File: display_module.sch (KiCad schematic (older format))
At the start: 110 parts, among them J3 F52R-1A7H1-11020, J4 46756-1001, Q3 BSS138APW, Q4 BSS138APW, Q5 BSS138APW, Q6 BSS138APW, U7 LT9611UXC, U8 NTS0102GT, Y1 ABM8G-24.000MHZ-18-D2Y-T

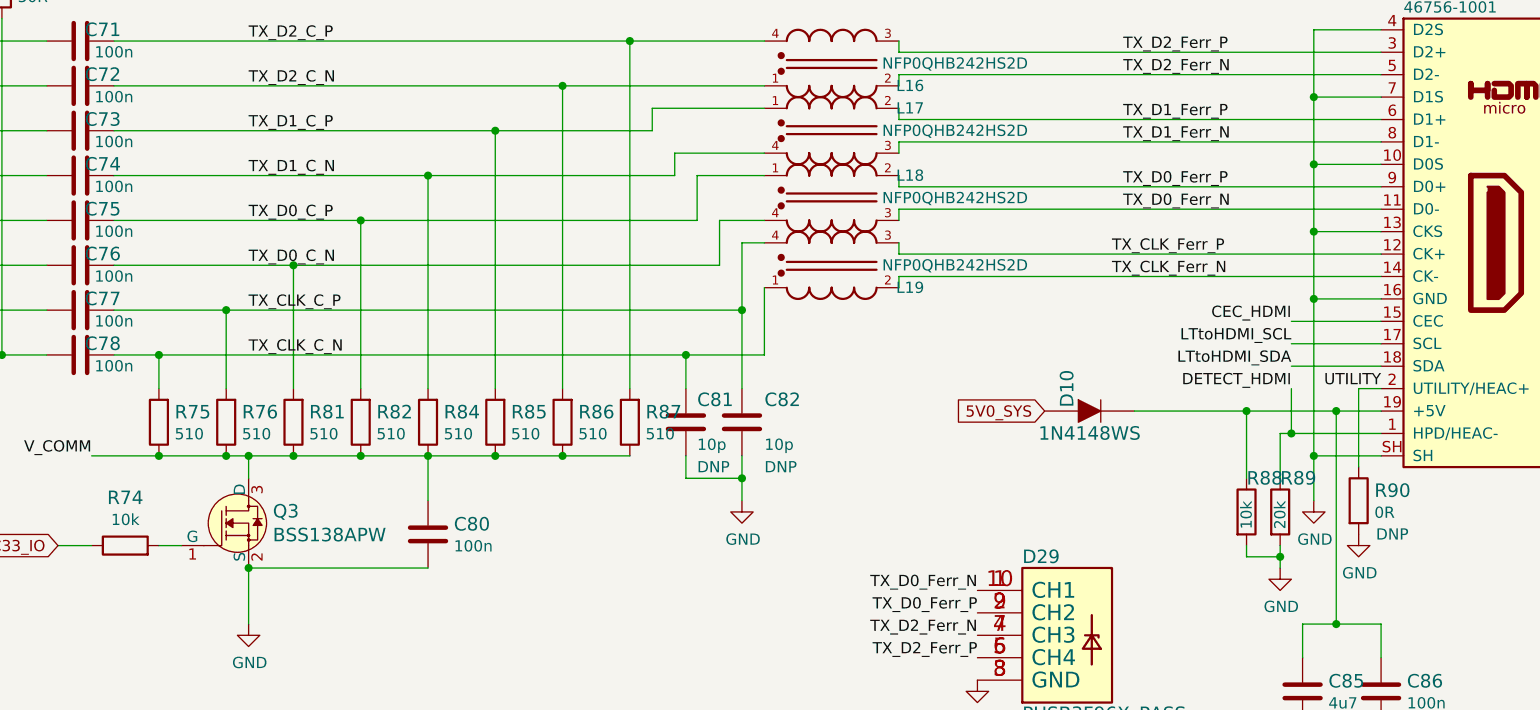
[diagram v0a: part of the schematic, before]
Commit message: Adjusted HDMI-side layout around Lontium chip
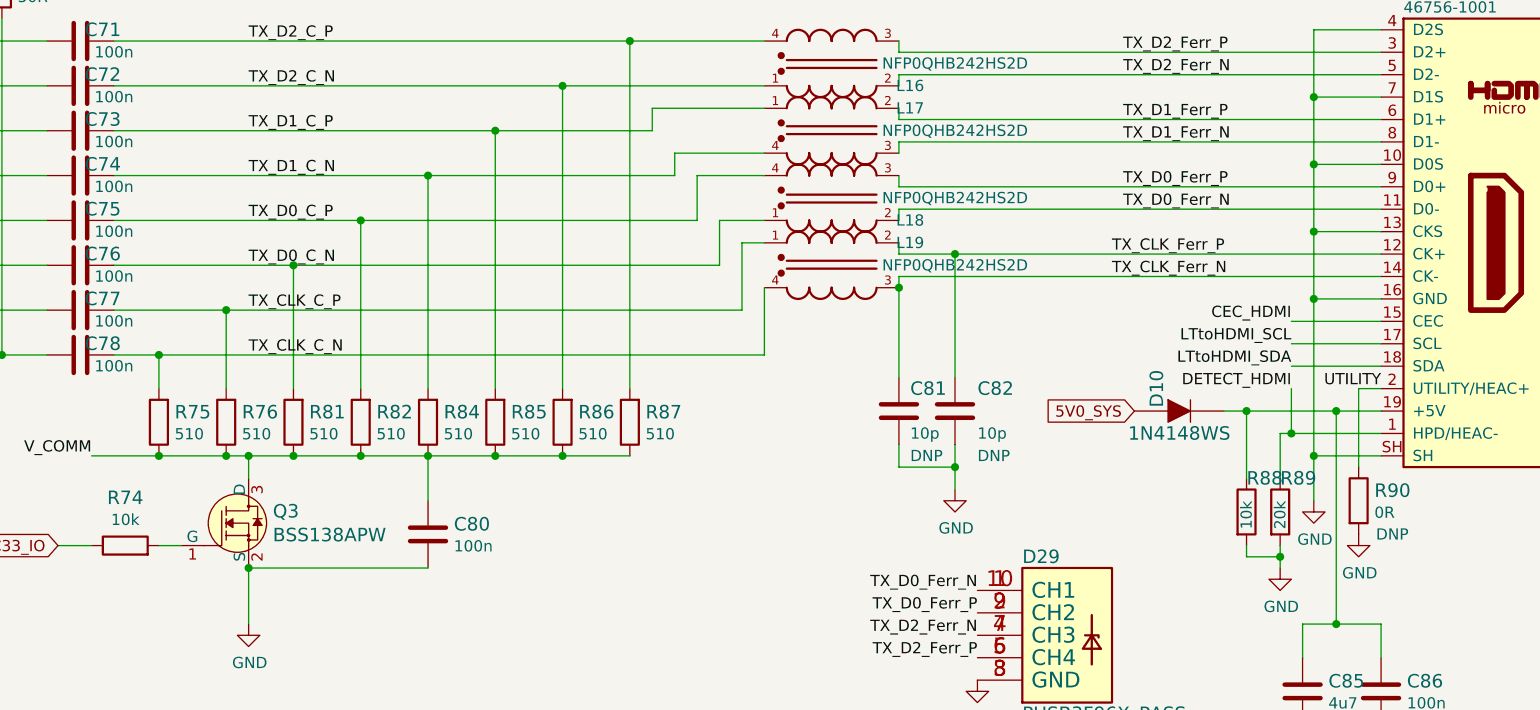
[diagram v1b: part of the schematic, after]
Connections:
- net TX_CLK_C_N: now also L19.4; no longer C81.1, L19.1
- net TX_CLK_C_P: now also L19.1; no longer C82.1, L19.4
- net TX_CLK_Ferr_N: now also C81.1, L19.3; no longer L19.2
- net TX_CLK_Ferr_P: now also C82.1, L19.2; no longer L19.3
- net TX_D0_C_N: now also L18.1; no longer L18.4
- net TX_D0_C_P: now also L18.4; no longer L18.1
- net TX_D0_Ferr_N: now also L18.2; no longer L18.3
- net TX_D0_Ferr_P: now also L18.3; no longer L18.2
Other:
- moved on the sheet: C81, C82, D10
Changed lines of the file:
@@
 F 5 "MURATA" H 12700 2126 50  0001 C CNN "Manufacturer"
 	1    12700 1900
-	1    0    0    -1
+	1    0    0    1
 $EndComp
 Wire Wire Line
@@
 F 5 "MURATA" H 12700 2426 50  0001 C CNN "Manufacturer"
 	1    12700 2200
-	1    0    0    1
+	1    0    0    -1
 $EndComp
 Wire Wire Line
@@
 L sc606-baseboard:C_10p_0402 C81
 U 1 1 64B46E2F
-P 12050 2900
-F 0 "C81" H 12100 3000 60  0000 L CNN
-F 1 "C_10p_0402" H 12050 2750 60  0001 C CNN
-F 2 "sc606-baseboard-footprints:0402-cap" H 12250 3100 60  0001 L CNN
-F 3 "" H 12050 2900 50  0001 C CNN
-F 4 "MULTICOMP" H 12250 3300 60  0001 L CNN "Manufacturer"
-F 5 "MC0402N100D500CT" H 12250 3200 60  0001 L CNN "MPN"
-F 6 "10p" H 12100 2800 50  0000 L CNN "Val"
-F 7 "DNP" H 12100 2700 50  0000 L CNN "DNP"
-	1    12050 2900
-	1    0    0    -1
-$EndComp
-Wire Wire Line
-	12050 2750 12050 2600
-Wire Wire Line
-	12300 2750 12300 2400
-Connection ~ 12300 2400
+P 13000 2850
+F 0 "C81" H 13050 2950 60  0000 L CNN
+F 1 "C_10p_0402" H 13000 2700 60  0001 C CNN
+F 2 "sc606-baseboard-footprints:0402-cap" H 13200 3050 60  0001 L CNN
+F 3 "" H 13000 2850 50  0001 C CNN
+F 4 "MULTICOMP" H 13200 3250 60  0001 L CNN "Manufacturer"
+F 5 "MC0402N100D500CT" H 13200 3150 60  0001 L CNN "MPN"
+F 6 "10p" H 13050 2750 50  0000 L CNN "Val"
+F 7 "DNP" H 13050 2650 50  0000 L CNN "DNP"
+	1    13000 2850
+	1    0    0    -1
+$EndComp
+Wire Wire Line
+	13000 2700 13000 2300
+Wire Wire Line
+	13250 2700 13250 2150
 Wire Wire Line
 	10000 2400 12300 2400
-Connection ~ 12050 2600
-Wire Wire Line
-	12050 2600 12400 2600
-Wire Wire Line
-	9700 2600 12050 2600
 $Comp
 L sc606-baseboard:GND #PWR077
 U 1 1 64CA82FA
-P 12300 3250
-F 0 "#PWR077" H 12300 3000 50  0001 C CNN
-F 1 "GND" H 12305 3077 50  0000 C CNN
-F 2 "" H 12300 3250 50  0001 C CNN
-F 3 "" H 12300 3250 50  0001 C CNN
-	1    12300 3250
-	1    0    0    -1
-$EndComp
-Wire Wire Line
-	12300 3250 12300 3150
-Wire Wire Line
-	12050 3150 12300 3150
-Connection ~ 12300 3150
-Wire Wire Line
-	12300 3150 12300 3050
-Wire Wire Line
-	12050 3150 12050 3050
+P 13250 3200
+F 0 "#PWR077" H 13250 2950 50  0001 C CNN
+F 1 "GND" H 13255 3027 50  0000 C CNN
+F 2 "" H 13250 3200 50  0001 C CNN
+F 3 "" H 13250 3200 50  0001 C CNN
+	1    13250 3200
+	1    0    0    -1
+$EndComp
+Wire Wire Line
+	13250 3200 13250 3100
+Wire Wire Line
+	13000 3100 13250 3100
+Connection ~ 13250 3100
+Wire Wire Line
+	13250 3100 13250 3000
+Wire Wire Line
+	13000 3100 13000 3000
 $Comp
 L sc606-baseboard:C_10p_0402 C82
 U 1 1 64B47860
-P 12300 2900
-F 0 "C82" H 12400 3000 60  0000 L CNN
-F 1 "C_10p_0402" H 12300 2750 60  0001 C CNN
-F 2 "sc606-baseboard-footprints:0402-cap" H 12500 3100 60  0001 L CNN
-F 3 "" H 12300 2900 50  0001 C CNN
-F 4 "MULTICOMP" H 12500 3300 60  0001 L CNN "Manufacturer"
-F 5 "MC0402N100D500CT" H 12500 3200 60  0001 L CNN "MPN"
-F 6 "10p" H 12400 2800 50  0000 L CNN "Val"
-F 7 "DNP" H 12400 2700 50  0000 L CNN "DNP"
-	1    12300 2900
+P 13250 2850
+F 0 "C82" H 13350 2950 60  0000 L CNN
+F 1 "C_10p_0402" H 13250 2700 60  0001 C CNN
+F 2 "sc606-baseboard-footprints:0402-cap" H 13450 3050 60  0001 L CNN
+F 3 "" H 13250 2850 50  0001 C CNN
+F 4 "MULTICOMP" H 13450 3250 60  0001 L CNN "Manufacturer"
+F 5 "MC0402N100D500CT" H 13450 3150 60  0001 L CNN "MPN"
+F 6 "10p" H 13350 2750 50  0000 L CNN "Val"
+F 7 "DNP" H 13350 2650 50  0000 L CNN "DNP"
+	1    13250 2850
 	1    0    0    -1
 $EndComp
@@
 Text Label 15150 2750 2    50   ~ 0
 UTILITY
-Text GLabel 13650 2850 0    50   Input ~ 0
+Text GLabel 14050 2850 0    50   Input ~ 0
 5V0_SYS
 $Comp
 L sc606-baseboard:1N4148WS D10
 U 1 1 620F4BEE
-P 13850 2850
-F 0 "D10" V 13750 2950 60  0000 C CNN
-F 1 "1N4148WS" H 13850 2750 60  0000 C CNN
-F 2 "sc606-baseboard-footprints:SOD-323F" H 14050 3050 60  0001 L CNN
-F 3 "https://www.onsemi.com/pub/Collateral/1N914BWS-D.pdf" H 14050 3150 60  0001 L CNN
-F 4 "1N4148WS" H 14050 3350 60  0001 L CNN "MPN"
-F 5 "ON Semiconductor" H 14050 3950 60  0001 L CNN "Manufacturer"
-	1    13850 2850
-	1    0    0    -1
-$EndComp
-Wire Wire Line
-	14050 2850 14550 2850
+P 14250 2850
+F 0 "D10" V 14150 2950 60  0000 C CNN
+F 1 "1N4148WS" H 14250 2750 60  0000 C CNN
+F 2 "sc606-baseboard-footprints:SOD-323F" H 14450 3050 60  0001 L CNN
+F 3 "https://www.onsemi.com/pub/Collateral/1N914BWS-D.pdf" H 14450 3150 60  0001 L CNN
+F 4 "1N4148WS" H 14450 3350 60  0001 L CNN "MPN"
+F 5 "ON Semiconductor" H 14450 3950 60  0001 L CNN "Manufacturer"
+	1    14250 2850
+	1    0    0    -1
+$EndComp
+Wire Wire Line
+	14450 2850 14550 2850
 Connection ~ 6900 1200
 Wire Wire Line
@@
 $EndComp
 Wire Wire Line
-	13000 2150 15150 2150
+	13000 2150 13250 2150
 Wire Wire Line
 	13000 1650 15150 1650
@@
 	1    0    0    -1
 $EndComp
+Wire Wire Line
+	9700 2600 12400 2600
+Connection ~ 13000 2300
+Connection ~ 13250 2150
+Wire Wire Line
+	13250 2150 15150 2150
 $EndSCHEMATC

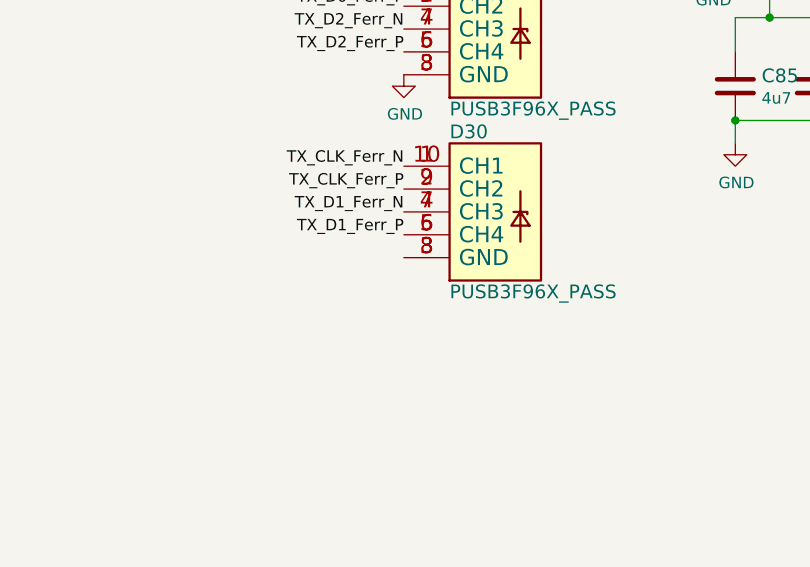
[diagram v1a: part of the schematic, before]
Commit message: Tuning CSI an HDMI traacks
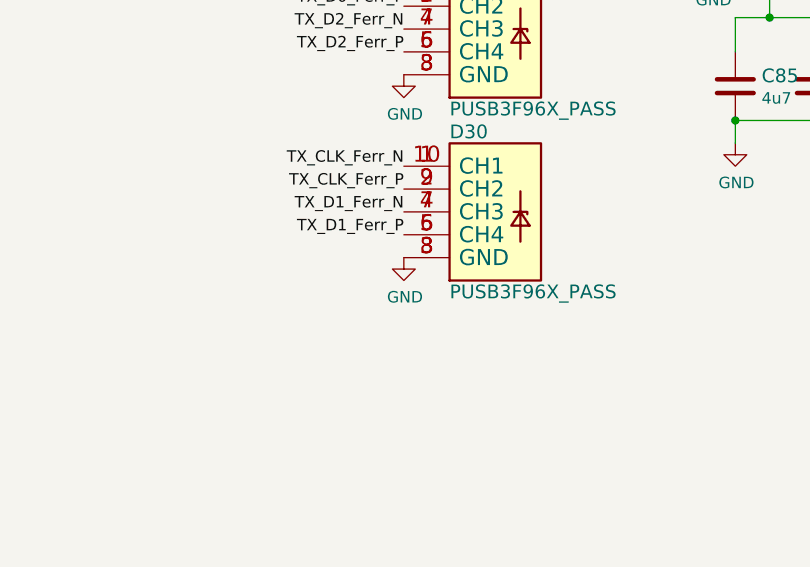
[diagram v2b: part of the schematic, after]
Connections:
- net GND: now also D30.3 (GND), D30.8 (GND)
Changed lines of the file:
@@
 Wire Wire Line
 	13250 2150 15150 2150
+$Comp
+L sc606-baseboard:GND #PWR0201
+U 1 1 620CB8A0
+P 13350 4850
+F 0 "#PWR0201" H 13350 4600 50  0001 C CNN
+F 1 "GND" H 13355 4677 50  0000 C CNN
+F 2 "" H 13350 4850 50  0001 C CNN
+F 3 "" H 13350 4850 50  0001 C CNN
+	1    13350 4850
+	1    0    0    -1
+$EndComp
 $EndSCHEMATC

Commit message: Cleaned display sch
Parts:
- removed J3: F52R-1A7H1-11020, sc606-baseboard-footprints:F52R-1A7H1-11020, symbol sc606-baseboard:F52R-1A7H1-11020
- added J3: F52R-1A7H1-11020, antmicro-footprints:F52R-1A7H1-11020, symbol antmicroFCCConnectors:F52R-1A7H1-11020
- added TP? (x4): TP, antmicro-footprints:TP-R-1.5, symbol antmicroTestPoints:TP
- C47, C64, C66: DNP DNP -> (none)
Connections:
- wire segments 375 -> 448
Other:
- note added: "Display - HDMI and LCD interfaces"
- note added: "MIPI DSI to HDMI"
- note removed: "MIPI DSI to HDMI\n"
- moved on the sheet: C46, C47, C48, C49, C50, C51, C52, C53, C54, C55, C56, C57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

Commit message: Added schema for serial interface connectors
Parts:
- J3: footprint antmicro-footprints:F52R-1A7H1-11020 -> sc606-baseboard-footprints:F52R-1A7H1-11020; symbol antmicroFCCConnectors:F52R-1A7H1-11020 -> sc606-baseboard:F52R-1A7H1-11020
- TP67, TP68, TP69, TP70: renamed from TP?; footprint antmicro-footprints:TP-R-1.5 -> sc606-baseboard-footprints:TP-R-1.5; symbol antmicroTestPoints:TP -> sc606-baseboard:TP-antmicroTestPoints

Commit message: Schematic cleanup
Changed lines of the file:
@@
 	2225 5550 2225 5525
-Wire Wire Line
-	4900 5600 4900 5650
 Wire Wire Line
 	4050 5550 4050 5250

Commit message: Update the sch signage, remove redundant sheets
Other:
- note removed: "Display - HDMI and LCD interfaces"
- moved on the sheet: C46, C47, C48, C49, C50, C51, C52, C53, C54, C55, C56, C57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
